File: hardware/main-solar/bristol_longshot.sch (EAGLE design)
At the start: 69 parts, among them U1 SAM_D20E, U10 LD6836TD/23P, U11 TPS73118DBVT, U2 SI4060, U3 UBLOX_MAX, U4 SST25WF040BT-40I/NP, U5 TG-5006CJ, U6 LTC3105EDDPBF, U7 TPS3123, U8 SN74LVC1G32DCKR, U9 BMP180

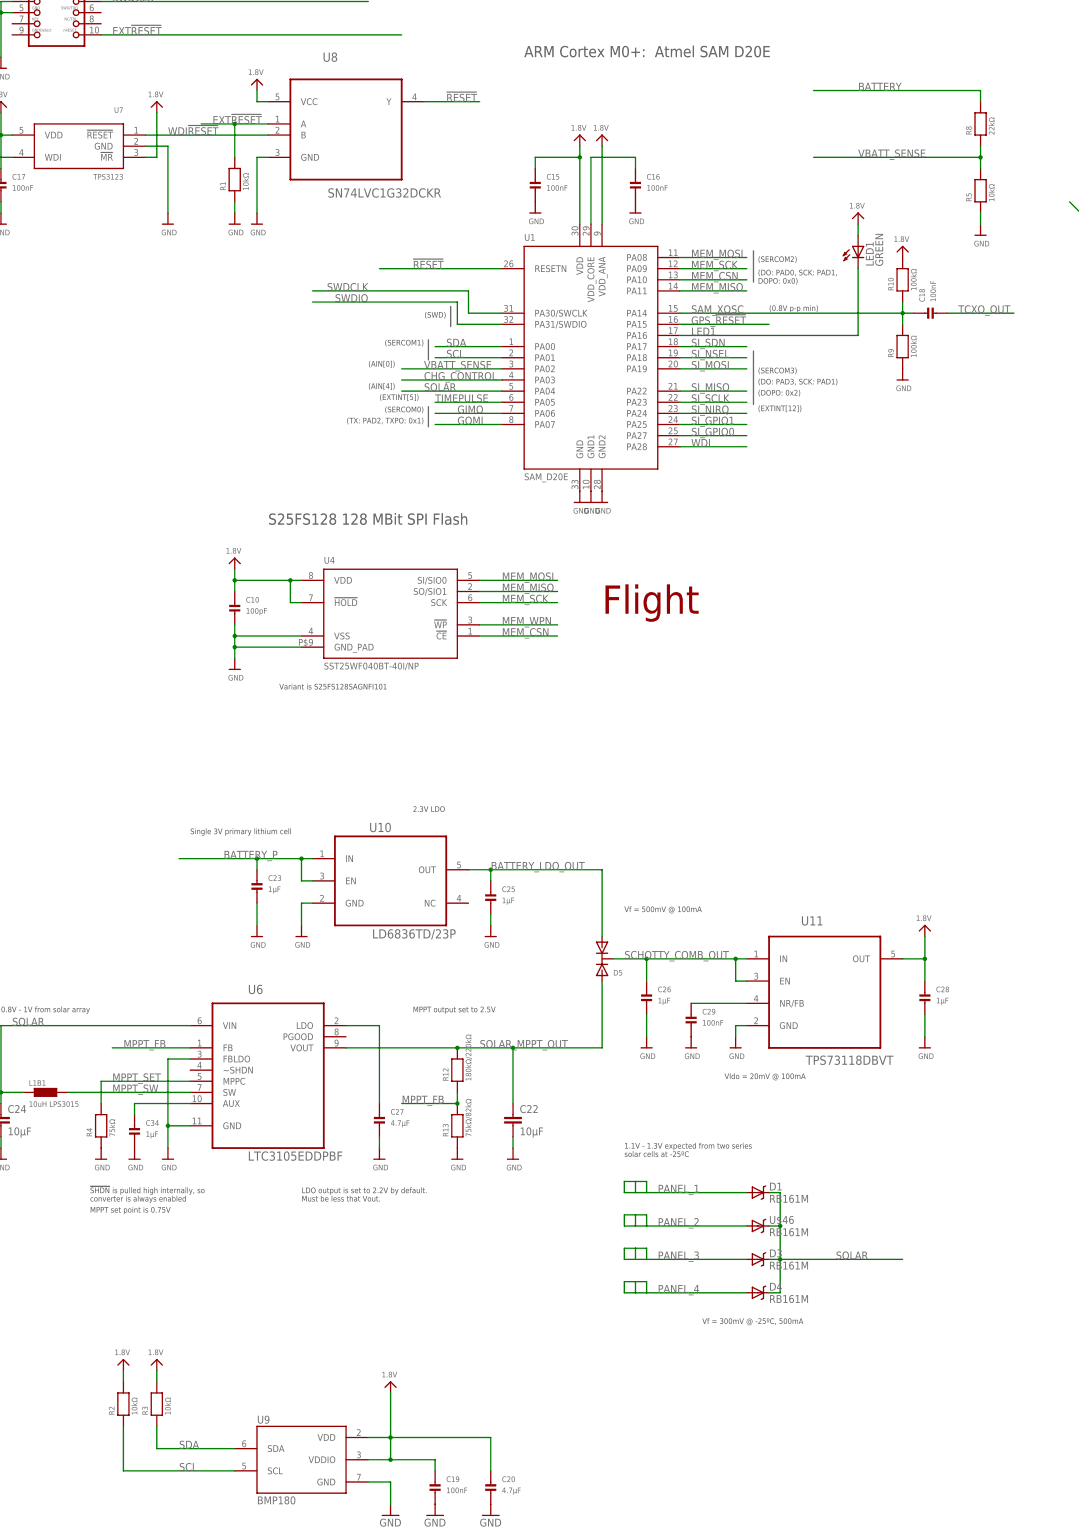
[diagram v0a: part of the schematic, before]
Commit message: More work on LTC3105 / primary 3V lithium board. Still work in progress
Needs solder pads and switch for 3V lithium battery.
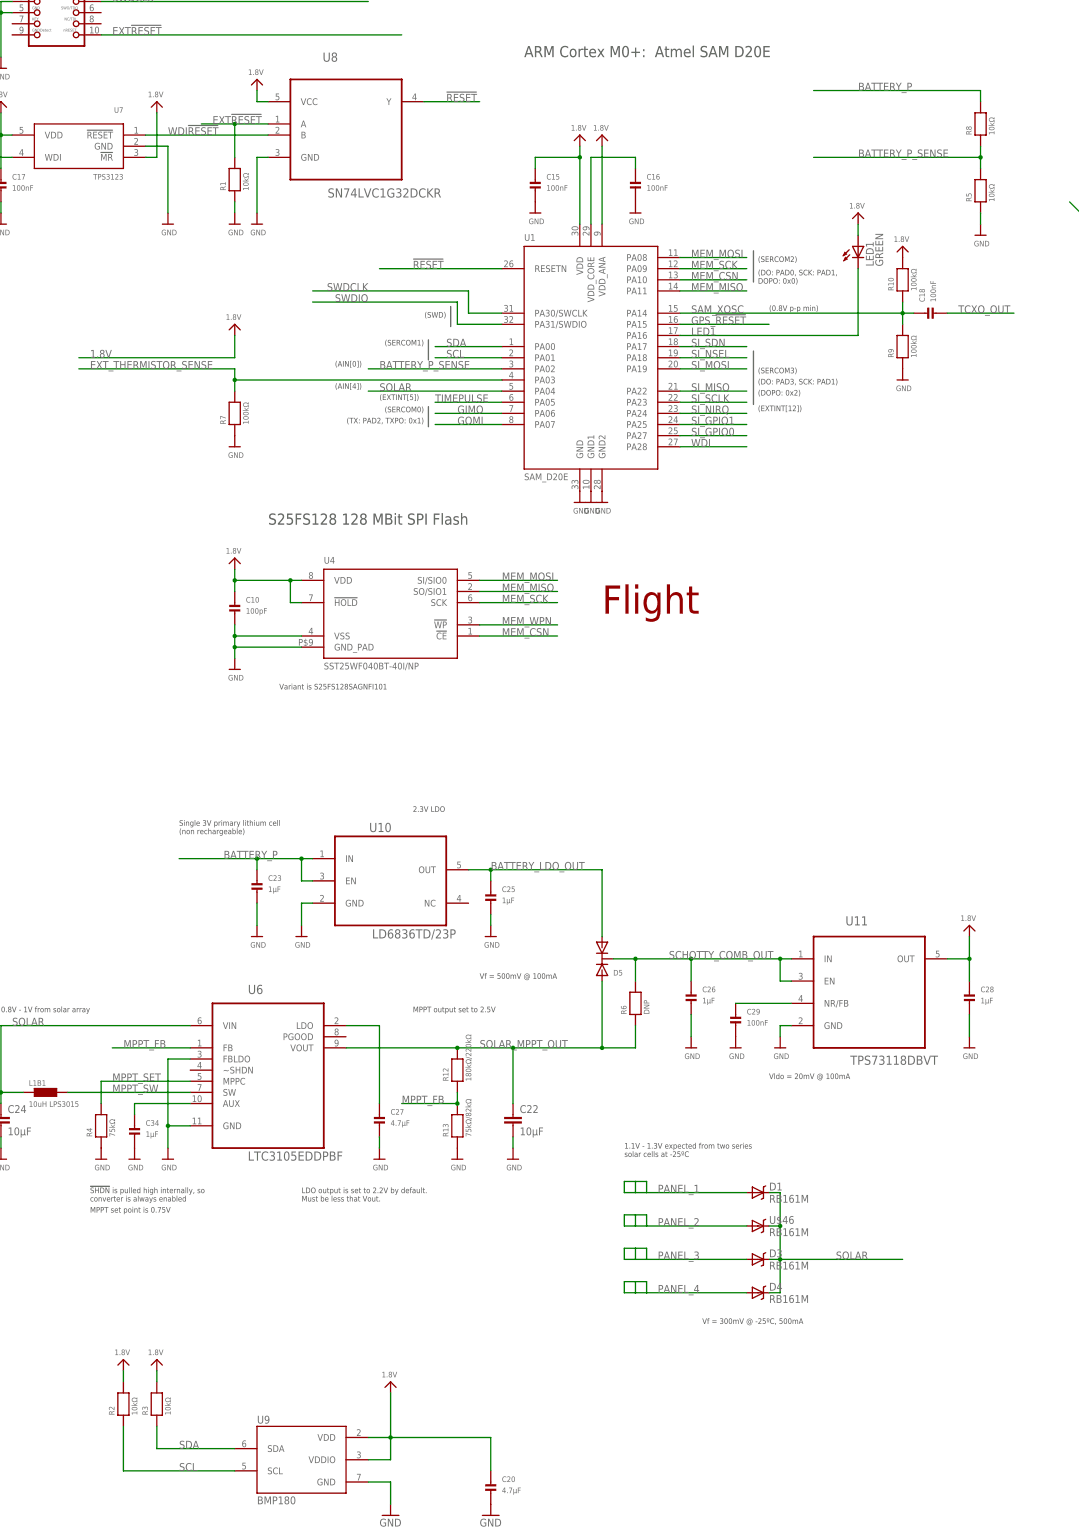
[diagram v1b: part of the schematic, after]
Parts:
- removed C19: 100nF, microbuilder_v3:CAP_CERAMIC_0402
- added R6: DNP, microbuilder_v3:RESISTOR_0402
- added R7: 100kΩ, microbuilder_v3:RESISTOR_0402
- R8: value 22kΩ -> 10kΩ
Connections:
- net VBATT_SENSE renamed BATTERY_P_SENSE
- removed net BATTERY: R8.2
- removed net CHG_CONTROL: U1.PA03
- new net EXT_THERMISTOR_SENSE: R7.2, U1.PA03
- net 1.8V: no longer C19.P$1
- net BATTERY_P: now also R8.2
- net GND: now also R7.1; no longer C19.P$2
- net SCHOTTY_COMB_OUT: now also R6.2
- net SOLAR_MPPT_OUT: now also R6.1
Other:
- note added: "Single 3V primary lithium cell (non rechargeable)"
- note removed: "Single 3V primary lithium cell"
- moved on the sheet: C26, C28, C29, U11
